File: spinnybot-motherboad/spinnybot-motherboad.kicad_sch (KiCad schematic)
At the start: 3 parts

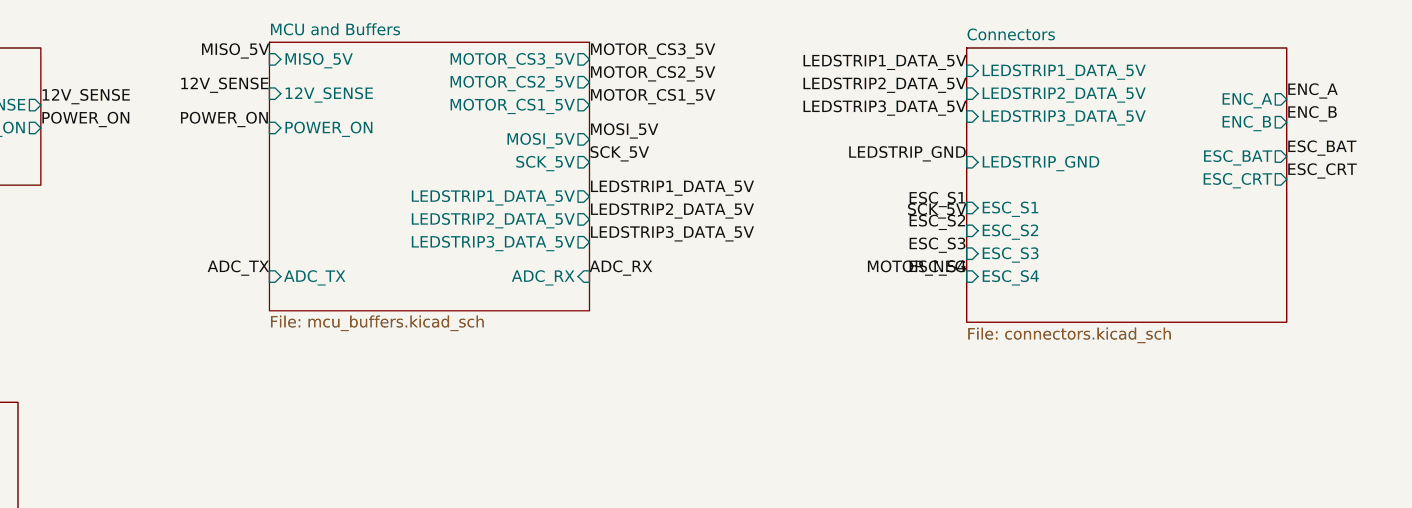
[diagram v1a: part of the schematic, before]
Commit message: Made ESP32 connections, added logic level shifter
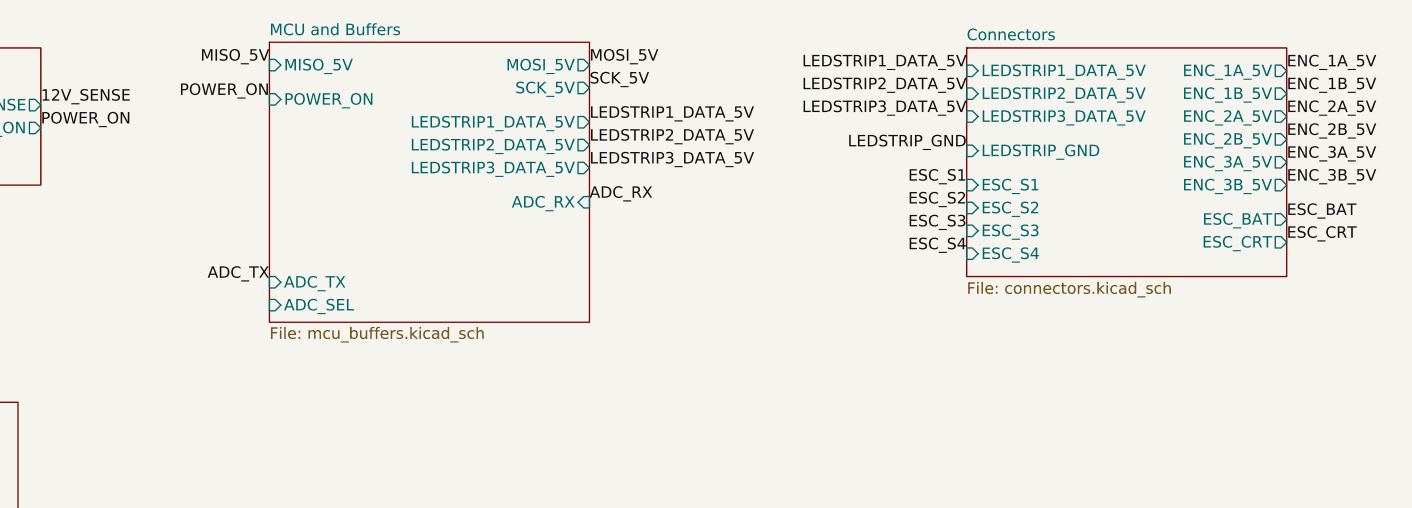
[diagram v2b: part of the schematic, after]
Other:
- sheet Connectors ports: added ENC_1A_5V, ENC_1B_5V, ENC_2A_5V, ENC_2B_5V, ENC_3A_5V, ENC_3B_5V; removed ENC_A, ENC_B
- sheet MCU and Buffers ports: added ADC_SEL; removed 12V_SENSE, MOTOR_CS1_5V, MOTOR_CS2_5V, MOTOR_CS3_5V

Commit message: PCB schematic (hopefully) finished
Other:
- sheet Connectors ports: added none; removed ESC_S4
- sheet IMU and Accelerometers ports: added ACCEL1_STATUS, ACCEL2_STATUS, ACCEL_SELF_TEST, ADC1_DRDY, ADC2_DRDY, ADC_RX, ADC_SEL, ADC_TX, IMU_CS, MISO_3V3, MOSI_3V3, SCK_3V3; removed none
- sheet MCU and Buffers ports: added ENC_1A_5V, ENC_1B_5V, ENC_2A_5V, ENC_2B_5V, ENC_3A_5V, ENC_3B_5V, ESC_S1, ESC_S2, ESS_S3, IMU_CS, MISO_3V3, MOSI_3V3, SCK_3V3; removed MISO_5V, MOSI_5V, SCK_5V
- sheet Power ports: added none; removed 12V_SENSE

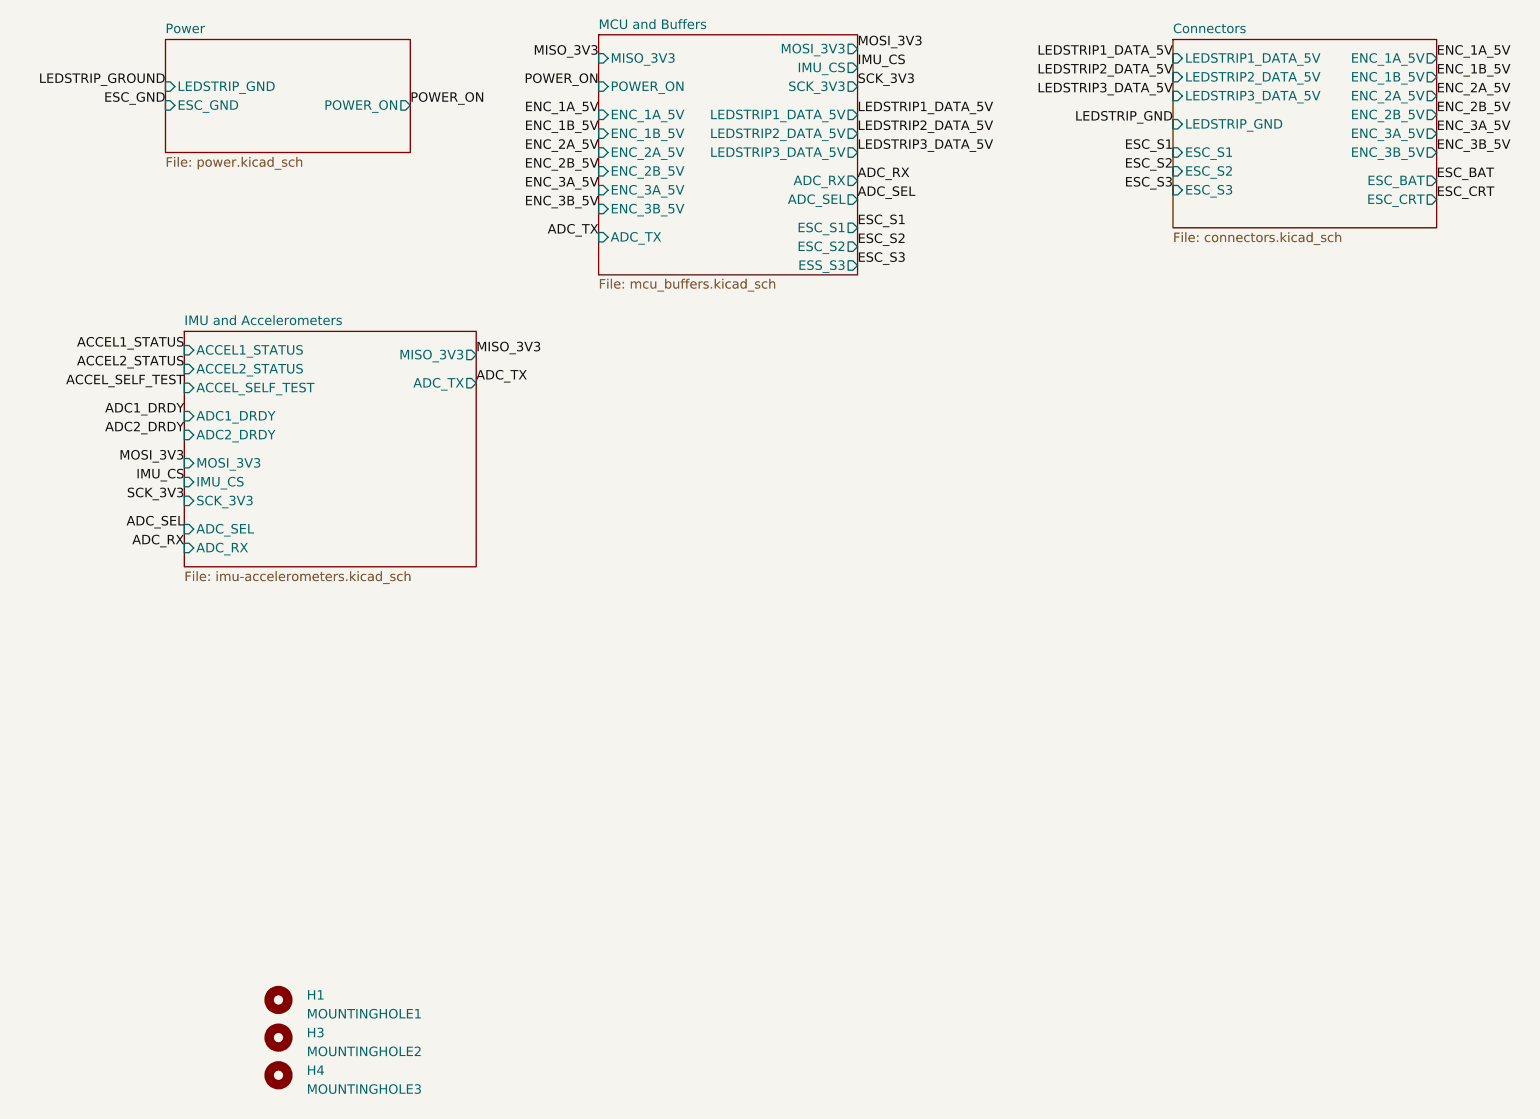
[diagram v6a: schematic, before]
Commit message: Power pads added, beginning routing
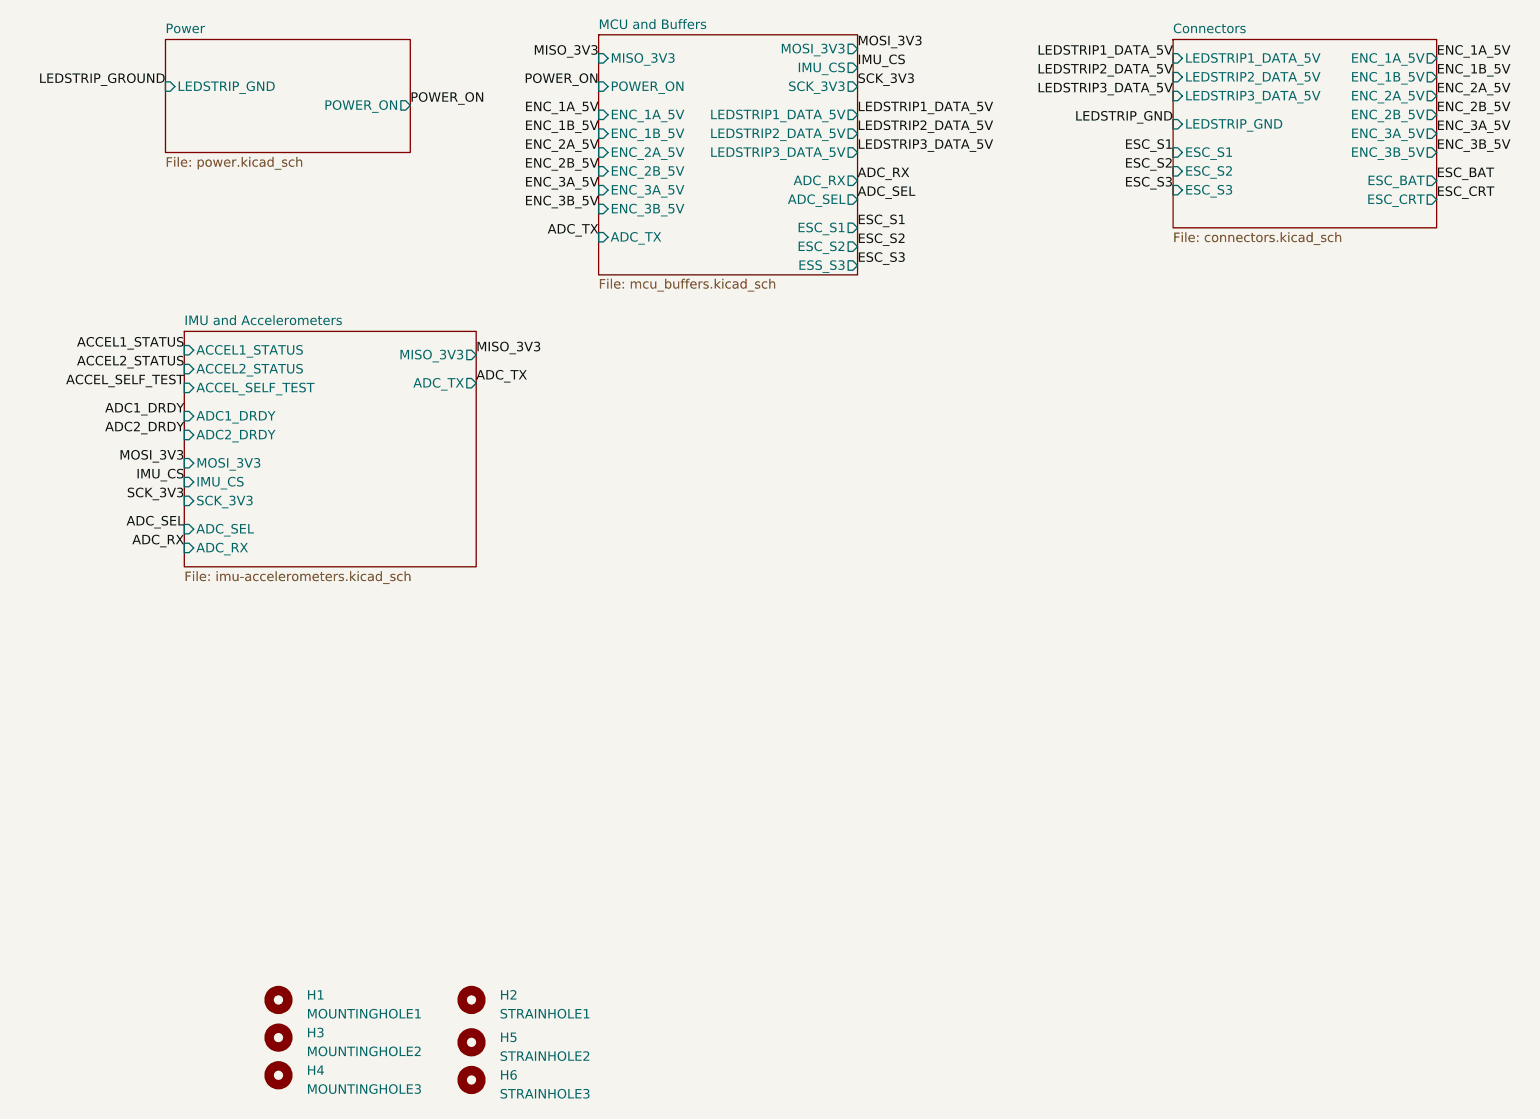
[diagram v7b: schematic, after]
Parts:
- added H2: STRAINHOLE1, custom:MountingHole_3.3mm, symbol Mechanical:MountingHole
- added H5: STRAINHOLE2, custom:MountingHole_3.3mm, symbol Mechanical:MountingHole
- added H6: STRAINHOLE3, custom:MountingHole_3.3mm, symbol Mechanical:MountingHole
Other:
- sheet Power ports: added none; removed ESC_GND
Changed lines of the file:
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@@
     (effects (font (size 1.27 1.27)) (justify left bottom))
-  )
-  (label "ESC_GND" (at 34.29 33.02 180)
-    (effects (font (size 1.27 1.27)) (justify right bottom))
   )
   (label "ENC_2B_5V" (at 92.71 41.91 180)
@@
     )
   )
+  (symbol (lib_id "Mechanical:MountingHole") (at 75.565 159.385 90) (unit 1)
+    (in_bom yes) (on_board yes)
+    (property "Reference" "H5" (id 0) (at 79.375 158.7499 90)
+      (effects (font (size 1.27 1.27)) (justify right))
+    )
+    (property "Value" "STRAINHOLE2" (id 1) (at 79.375 161.2899 90)
+      (effects (font (size 1.27 1.27)) (justify right))
+    )
+    (property "Footprint" "custom:MountingHole_3.3mm" (id 2) (at 75.565 159.385 0)
+      (effects (font (size 1.27 1.27)) hide)
+    )
+    (property "Datasheet" "~" (id 3) (at 75.565 159.385 0)
+      (effects (font (size 1.27 1.27)) hide)
+    )
+  )
   (symbol (lib_id "Mechanical:MountingHole") (at 49.53 163.83 90) (unit 1)
     (in_bom yes) (on_board yes)
@@
     )
     (property "Datasheet" "~" (id 3) (at 49.53 158.75 0)
+      (effects (font (size 1.27 1.27)) hide)
+    )
+  )
+  (symbol (lib_id "Mechanical:MountingHole") (at 75.565 153.67 90) (unit 1)
+    (in_bom yes) (on_board yes)
+    (property "Reference" "H2" (id 0) (at 79.375 153.0349 90)
+      (effects (font (size 1.27 1.27)) (justify right))
+    )
+    (property "Value" "STRAINHOLE1" (id 1) (at 79.375 155.5749 90)
+      (effects (font (size 1.27 1.27)) (justify right))
+    )
+    (property "Footprint" "custom:MountingHole_3.3mm" (id 2) (at 75.565 153.67 0)
+      (effects (font (size 1.27 1.27)) hide)
+    )
+    (property "Datasheet" "~" (id 3) (at 75.565 153.67 0)
+      (effects (font (size 1.27 1.27)) hide)
+    )
+  )
+  (symbol (lib_id "Mechanical:MountingHole") (at 75.565 164.465 90) (unit 1)
+    (in_bom yes) (on_board yes)
+    (property "Reference" "H6" (id 0) (at 79.375 163.8299 90)
+      (effects (font (size 1.27 1.27)) (justify right))
+    )
+    (property "Value" "STRAINHOLE3" (id 1) (at 79.375 166.3699 90)
+      (effects (font (size 1.27 1.27)) (justify right))
+    )
+    (property "Footprint" "custom:MountingHole_3.3mm" (id 2) (at 75.565 164.465 0)
+      (effects (font (size 1.27 1.27)) hide)
+    )
+    (property "Datasheet" "~" (id 3) (at 75.565 164.465 0)
       (effects (font (size 1.27 1.27)) hide)
     )
@@
     (pin "POWER_ON" output (at 67.31 33.02 0)
       (effects (font (size 1.27 1.27)) (justify right))
-    )
-    (pin "ESC_GND" input (at 34.29 33.02 180)
-      (effects (font (size 1.27 1.27)) (justify left))
     )
   )
@@
       (reference "#PWR0157") (unit 1) (value "GND") (footprint "")
     )
+    (path "/a01fd824-f54b-4196-9957-3a30a77eb56a/1fb341b7-0ae8-49b7-8f4d-fa9dfaf3f00f"
+      (reference "#PWR0158") (unit 1) (value "GND") (footprint "")
+    )
     (path "/dd1316dc-7e5b-4c97-959e-6f6a1eeeb379/b5ccd461-2bb6-4e55-889d-c413ead53e97"
       (reference "C1") (unit 1) (value "10u") (footprint "Capacitor_SMD:C_1206_3216Metric_Pad1.33x1.80mm_HandSolder")
@@
       (reference "H1") (unit 1) (value "MOUNTINGHOLE1") (footprint "custom:MountingHole_3.3mm")
     )
+    (path "/90a0860f-dc0f-486d-8126-ac86f257452e"
+      (reference "H2") (unit 1) (value "STRAINHOLE1") (footprint "custom:MountingHole_3.3mm")
+    )
     (path "/4daec26f-7303-4f29-a6dc-74eca012aa20"
       (reference "H3") (unit 1) (value "MOUNTINGHOLE2") (footprint "custom:MountingHole_3.3mm")
@@
       (reference "H4") (unit 1) (value "MOUNTINGHOLE3") (footprint "custom:MountingHole_3.3mm")
     )
+    (path "/44671e4b-c3f2-40ce-9f5f-ae56c7ceee2e"
+      (reference "H5") (unit 1) (value "STRAINHOLE2") (footprint "custom:MountingHole_3.3mm")
+    )
+    (path "/b2df31ea-f8d8-459e-bfc0-eb9493f3925c"
+      (reference "H6") (unit 1) (value "STRAINHOLE3") (footprint "custom:MountingHole_3.3mm")
+    )
     (path "/ce9f0f17-1862-4671-a57d-feb3cf47b091/205531ef-2109-472f-bb9a-44bf26b6d265"
       (reference "J1") (unit 1) (value "ENCODER 1") (footprint "S4B-PH-SM4-TB:S4B-PH-SM4-TBLFSN")
@@
       (reference "J7") (unit 1) (value "SM10B-SRSS-TB") (footprint "esc_4in1:SM10B-SRSS-TB")
     )
+    (path "/a01fd824-f54b-4196-9957-3a30a77eb56a/41e14b01-c483-4e24-95ec-8abc5377731f"
+      (reference "J8") (unit 1) (value "BAT_POS") (footprint "Connector_Wire:SolderWirePad_1x01_SMD_5x10mm")
+    )
     (path "/a01fd824-f54b-4196-9957-3a30a77eb56a/a923e568-7e66-4b54-9b31-57960a65fa25"
       (reference "J9") (unit 1) (value "POWER SW1") (footprint "Connector_JST:JST_PH_S2B-PH-SM4-TB_1x02-1MP_P2.00mm_Horizontal")
     )
+    (path "/a01fd824-f54b-4196-9957-3a30a77eb56a/21a22a9e-8cdd-4970-8092-31ac5119bd77"
+      (reference "J10") (unit 1) (value "ESC_POS") (footprint "custom:Stitched_SolderWirePad_1x01_SMD_5x10mm")
+    )
     (path "/a01fd824-f54b-4196-9957-3a30a77eb56a/914db2dc-fdb3-4d66-9e7f-79c06cd2d446"
       (reference "J11") (unit 1) (value "POWER SW2") (footprint "Connector_JST:JST_PH_S2B-PH-SM4-TB_1x02-1MP_P2.00mm_Horizontal")
@@
       (reference "J14") (unit 1) (value "LEDSTRIP3") (footprint "B3B-PH-SM4:JST_B3B-PH-SM4-TB(LF)(SN)")
     )
+    (path "/a01fd824-f54b-4196-9957-3a30a77eb56a/293e9033-d210-43c3-a3d4-7d01a9d750c0"
+      (reference "J15") (unit 1) (value "BAT_GND") (footprint "custom:Stitched_SolderWirePad_1x01_SMD_5x10mm")
+    )
+    (path "/a01fd824-f54b-4196-9957-3a30a77eb56a/b6e3a65a-850d-4c23-a22a-c94323487d53"
+      (reference "J16") (unit 1) (value "ESC_GND") (footprint "Connector_Wire:SolderWirePad_1x01_SMD_5x10mm")
+    )
     (path "/dd1316dc-7e5b-4c97-959e-6f6a1eeeb379/cd41de04-53db-49dd-9870-c7e12fdc7cf9"
